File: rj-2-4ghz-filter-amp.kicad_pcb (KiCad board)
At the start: 4 copper layers, 114.3 x 63.5 mm, 80 parts, among them IC1 MP1584EN-LF-Z, IC2 MP1584EN-LF-Z, J2 Barrel_Jack, J3 Conn_01x03, J4 Conn_01x03, J5 Conn_01x03, J6 Conn_01x03, J7 Conn_01x02, J8 Conn_01x02, J9 Conn_01x02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

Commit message: done till all routing ground ring and ground plane handeled, only bare copper part is left
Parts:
- added H1: MountingHole_Pad, MountingHole:MountingHole_3.2mm_M3_Pad_Via, F.Cu at (228.2, 48.0)
- added H2: MountingHole_Pad, MountingHole:MountingHole_3.2mm_M3_Pad_Via, F.Cu at (228.3, 118.5)
- added H3: MountingHole_Pad, MountingHole:MountingHole_3.2mm_M3_Pad_Via, F.Cu at (96.3, 118.5)
- added H4: MountingHole_Pad, MountingHole:MountingHole_3.2mm_M3_Pad_Via, F.Cu at (96.5, 47.9)
- added H7: MountingHole_Pad, MountingHole:MountingHole_3.2mm_M3_Pad_Via, F.Cu at (193.9, 68.1)
- added H8: MountingHole_Pad, MountingHole:MountingHole_3.2mm_M3_Pad_Via, F.Cu at (193.1, 110.8)
- J2: footprint Connector_BarrelJack:BarrelJack_Horizontal -> Connector_BarrelJack:BarrelJack_CLIFF_FC681465S_SMT_Horizontal
- J3, J4, J5, J6: footprint Connector_PinHeader_2.54mm:PinHeader_1x03_P2.54mm_Vertical -> Connector_PinHeader_2.54mm:PinHeader_1x03_P2.54mm_Vertical_SMD_Pin1Left
- J7, J8, J9: footprint Connector_PinHeader_2.54mm:PinHeader_1x02_P2.54mm_Vertical -> Connector_PinHeader_2.54mm:PinHeader_1x02_P2.54mm_Vertical_SMD_Pin1Left
- R7: value 50 -> 100
- R8: value 50 -> 100; footprint Resistor_SMD:R_0603_1608Metric_Pad1.05x0.95mm_HandSolder -> Resistor_SMD:R_2010_5025Metric_Pad1.52x2.65mm_HandSolder
- moved J8 28.1 mm to (190.2, 87.7)
- moved X2 27.9 mm to (230.5, 91.8)
- moved J6 26.3 mm to (180.4, 65.8)
- moved J7 24.1 mm to (173.9, 65.8)
- moved R8 21.6 mm to (206.7, 91.8)
- moved J5 21.0 mm to (165.1, 65.8)
- moved J4 18.9 mm to (158.0, 65.8)
- moved J3 16.7 mm to (150.9, 65.8)
- moved C10 16.6 mm to (191.8, 78.5)
- moved C11 16.6 mm to (184.7, 77.5)
- moved C12 16.6 mm to (185.5, 75.5)
- moved C13 16.6 mm to (178.5, 77.5)
- moved C14 16.6 mm to (177.8, 75.5)
- moved C17 16.6 mm to (183.8, 105.6)
- moved C18 16.6 mm to (179.5, 104.0)
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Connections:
- J2 pad 3: GND -> (no net)
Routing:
- net /High Power Ampifier/RF_IN: track 66.4 -> 122.5 mm
- net /High Power Ampifier/RF_OUT: track 94.4 -> 122.5 mm
- net GND: track 22.8 -> 50.5 mm, vias 137 -> 491
- net /5V_B1: track 33.7 -> 56.2 mm
- net /RF Attenuator/LE: track 42.6 -> 62.2 mm
- net /RF Attenuator/A0: track 56.9 -> 43.1 mm
- net Net-(J8-Pad2): track 5.06 -> 18.3 mm
- net /RF Attenuator/SI: track 45.8 -> 57.9 mm
- net /RF Attenuator/CLK: track 38.6 -> 50.3 mm
- net /RF Attenuator/A2: track 39.3 -> 49.7 mm
- net Net-(C6-Pad1): track 8.12 -> 15.6 mm
- net /5V_B2: track 23.4 -> 30.8 mm, vias 61 -> 60
- net /Buck 1 5v/PWR_IN: track 8.13 -> 4.76 mm, vias 45 -> 72
- net Net-(J9-Pad2): track 5.32 -> 8.67 mm
- net /RF Attenuator/A1: track 41.5 -> 41.0 mm, vias 2 -> 0
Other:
- board size 114.3 x 63.5 mm -> 142.2 x 80.3 mm
- board text added: "+12V"
- board text added: "G"

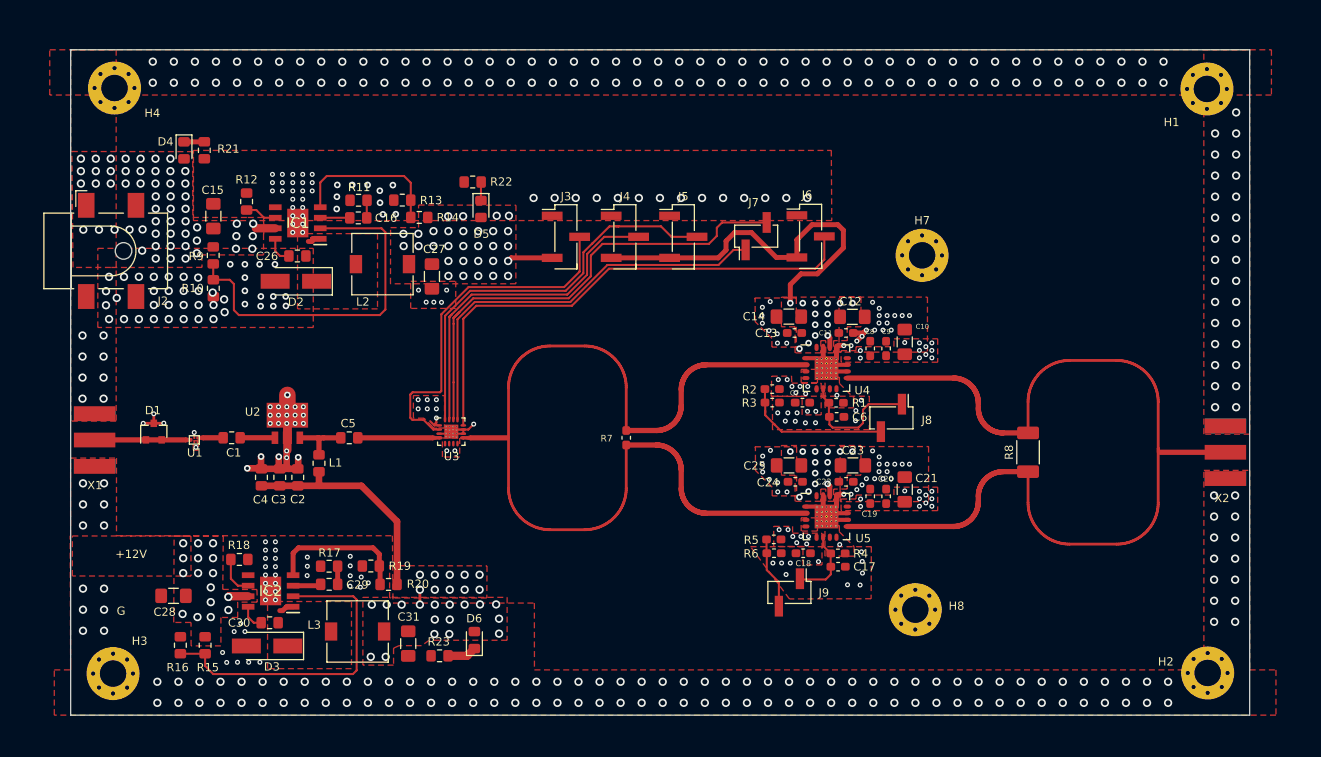
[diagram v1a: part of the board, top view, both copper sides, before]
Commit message: hole positionsing and few via fixing
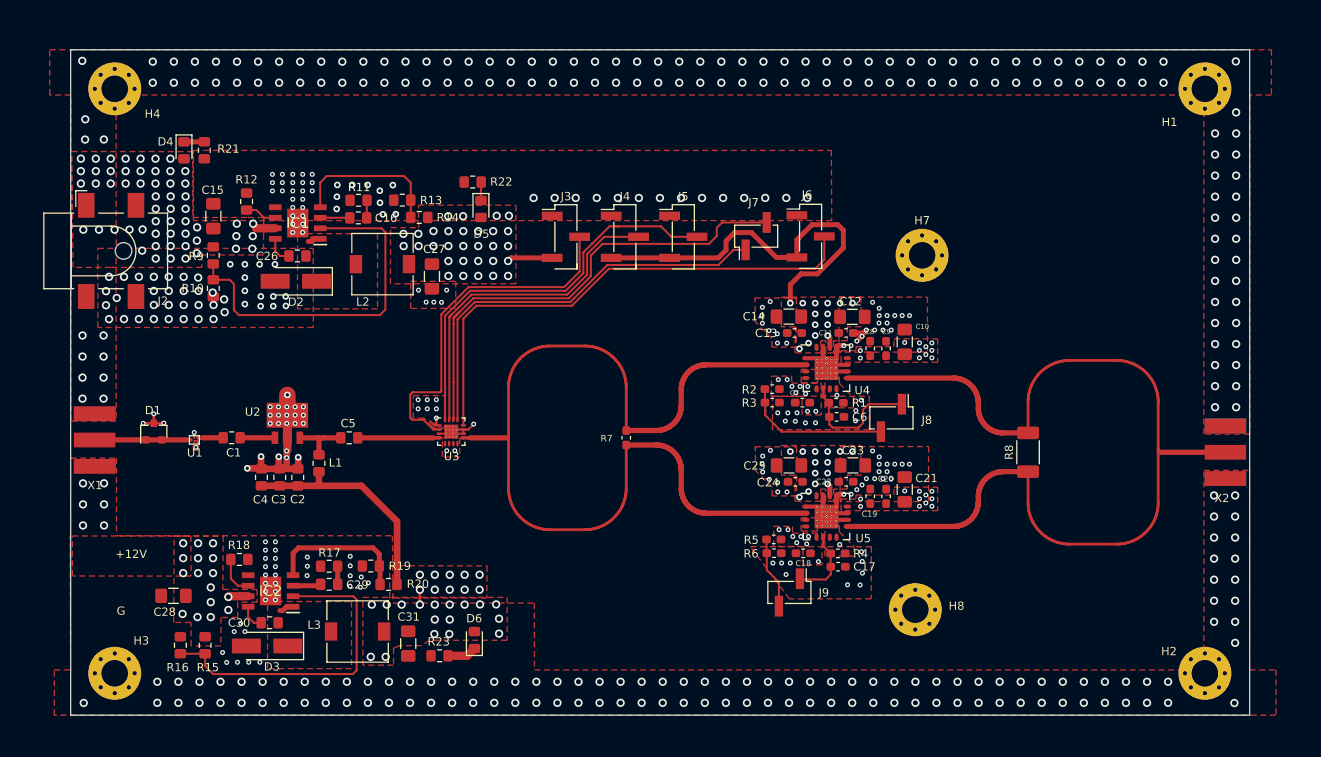
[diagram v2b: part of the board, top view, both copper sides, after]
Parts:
- moved H2 0.34 mm to (228.0, 118.5)
- moved H1 0.24 mm to (228.0, 48.0)
- moved H3 0.20 mm to (96.5, 118.5)
- moved H4 0.10 mm to (96.5, 48.0)
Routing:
- net GND: vias 491 -> 493
